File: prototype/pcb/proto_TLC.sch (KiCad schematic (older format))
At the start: 29 parts, among them Q1 RZM001P02, Q2 RZM001P02, Q3 RZM001P02, Q4 RZM001P02, U1 TLC5954

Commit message: Finished rectangular prototype board
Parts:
- renumbered C3 to C1, C1 to C2, C2 to C3, D4 to D10, D6 to D11, D8 to D12, D9 to D13, D11 to D14, D13 to D15, D15 to D16, D3 to D2, D5 to D3, D7 to D4, D10 to D5, D12 to D6, D14 to D7, D16 to D8, D2 to D9, R5 to R4, R4 to R5
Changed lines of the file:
@@
 $EndComp
 $Comp
-L APHB1608LVBDSEKJ3C D3
+L APHB1608LVBDSEKJ3C D2
 U 1 1 574E23F2
 P 6600 2850
-F 0 "D3" H 6400 3050 50  0000 L CNN
+F 0 "D2" H 6400 3050 50  0000 L CNN
 F 1 "APHB1608LVBDSEKJ3C" H 6550 2650 50  0000 C CNN
 F 2 "led:led_dual" H 6600 2800 60  0001 C CNN
@@
 $EndComp
 $Comp
-L APHB1608LVBDSEKJ3C D5
+L APHB1608LVBDSEKJ3C D3
 U 1 1 574E2426
 P 7200 2850
-F 0 "D5" H 7000 3050 50  0000 L CNN
+F 0 "D3" H 7000 3050 50  0000 L CNN
 F 1 "APHB1608LVBDSEKJ3C" H 7150 2650 50  0000 C CNN
 F 2 "led:led_dual" H 7200 2800 60  0001 C CNN
@@
 $EndComp
 $Comp
-L APHB1608LVBDSEKJ3C D7
+L APHB1608LVBDSEKJ3C D4
 U 1 1 574E245C
 P 7750 2850
-F 0 "D7" H 7550 3050 50  0000 L CNN
+F 0 "D4" H 7550 3050 50  0000 L CNN
 F 1 "APHB1608LVBDSEKJ3C" H 7700 2650 50  0000 C CNN
 F 2 "led:led_dual" H 7750 2800 60  0001 C CNN
@@
 $EndComp
 $Comp
-L APHB1608LVBDSEKJ3C D10
+L APHB1608LVBDSEKJ3C D5
 U 1 1 574E248E
 P 8350 2850
-F 0 "D10" H 8150 3050 50  0000 L CNN
+F 0 "D5" H 8150 3050 50  0000 L CNN
 F 1 "APHB1608LVBDSEKJ3C" H 8300 2650 50  0000 C CNN
 F 2 "led:led_dual" H 8350 2800 60  0001 C CNN
@@
 $EndComp
 $Comp
-L APHB1608LVBDSEKJ3C D12
+L APHB1608LVBDSEKJ3C D6
 U 1 1 574E24C0
 P 8900 2850
-F 0 "D12" H 8700 3050 50  0000 L CNN
+F 0 "D6" H 8700 3050 50  0000 L CNN
 F 1 "APHB1608LVBDSEKJ3C" H 8850 2650 50  0000 C CNN
 F 2 "led:led_dual" H 8900 2800 60  0001 C CNN
@@
 $EndComp
 $Comp
-L APHB1608LVBDSEKJ3C D14
+L APHB1608LVBDSEKJ3C D7
 U 1 1 574E38A4
 P 9500 2850
-F 0 "D14" H 9300 3050 50  0000 L CNN
+F 0 "D7" H 9300 3050 50  0000 L CNN
 F 1 "APHB1608LVBDSEKJ3C" H 9450 2650 50  0000 C CNN
 F 2 "led:led_dual" H 9500 2800 60  0001 C CNN
@@
 $EndComp
 $Comp
-L APHB1608LVBDSEKJ3C D16
+L APHB1608LVBDSEKJ3C D8
 U 1 1 574E38AA
 P 10050 2850
-F 0 "D16" H 9850 3050 50  0000 L CNN
+F 0 "D8" H 9850 3050 50  0000 L CNN
 F 1 "APHB1608LVBDSEKJ3C" H 10000 2650 50  0000 C CNN
 F 2 "led:led_dual" H 10050 2800 60  0001 C CNN
@@
 $EndComp
 $Comp
-L APHB1608LVBDSEKJ3C D2
+L APHB1608LVBDSEKJ3C D9
 U 1 1 574E38B0
 P 6050 4450
-F 0 "D2" H 5850 4650 50  0000 L CNN
+F 0 "D9" H 5850 4650 50  0000 L CNN
 F 1 "APHB1608LVBDSEKJ3C" H 6000 4250 50  0000 C CNN
 F 2 "led:led_dual" H 6050 4400 60  0001 C CNN
@@
 $EndComp
 $Comp
-L APHB1608LVBDSEKJ3C D4
+L APHB1608LVBDSEKJ3C D10
 U 1 1 574E38B6
 P 6600 4450
-F 0 "D4" H 6400 4650 50  0000 L CNN
+F 0 "D10" H 6400 4650 50  0000 L CNN
 F 1 "APHB1608LVBDSEKJ3C" H 6550 4250 50  0000 C CNN
 F 2 "led:led_dual" H 6600 4400 60  0001 C CNN
@@
 $EndComp
 $Comp
-L APHB1608LVBDSEKJ3C D6
+L APHB1608LVBDSEKJ3C D11
 U 1 1 574E38BC
 P 7200 4450
-F 0 "D6" H 7000 4650 50  0000 L CNN
+F 0 "D11" H 7000 4650 50  0000 L CNN
 F 1 "APHB1608LVBDSEKJ3C" H 7150 4250 50  0000 C CNN
 F 2 "led:led_dual" H 7200 4400 60  0001 C CNN
@@
 $EndComp
 $Comp
-L APHB1608LVBDSEKJ3C D8
+L APHB1608LVBDSEKJ3C D12
 U 1 1 574E38C2
 P 7750 4450
-F 0 "D8" H 7550 4650 50  0000 L CNN
+F 0 "D12" H 7550 4650 50  0000 L CNN
 F 1 "APHB1608LVBDSEKJ3C" H 7700 4250 50  0000 C CNN
 F 2 "led:led_dual" H 7750 4400 60  0001 C CNN
@@
 $EndComp
 $Comp
-L APHB1608LVBDSEKJ3C D9
+L APHB1608LVBDSEKJ3C D13
 U 1 1 574E41CA
 P 8300 4450
-F 0 "D9" H 8100 4650 50  0000 L CNN
+F 0 "D13" H 8100 4650 50  0000 L CNN
 F 1 "APHB1608LVBDSEKJ3C" H 8250 4250 50  0000 C CNN
 F 2 "led:led_dual" H 8300 4400 60  0001 C CNN
@@
 $EndComp
 $Comp
-L APHB1608LVBDSEKJ3C D11
+L APHB1608LVBDSEKJ3C D14
 U 1 1 574E41D0
 P 8850 4450
-F 0 "D11" H 8650 4650 50  0000 L CNN
+F 0 "D14" H 8650 4650 50  0000 L CNN
 F 1 "APHB1608LVBDSEKJ3C" H 8800 4250 50  0000 C CNN
 F 2 "led:led_dual" H 8850 4400 60  0001 C CNN
@@
 $EndComp
 $Comp
-L APHB1608LVBDSEKJ3C D13
+L APHB1608LVBDSEKJ3C D15
 U 1 1 574E41D6
 P 9450 4450
-F 0 "D13" H 9250 4650 50  0000 L CNN
+F 0 "D15" H 9250 4650 50  0000 L CNN
 F 1 "APHB1608LVBDSEKJ3C" H 9400 4250 50  0000 C CNN
 F 2 "led:led_dual" H 9450 4400 60  0001 C CNN
@@
 $EndComp
 $Comp
-L APHB1608LVBDSEKJ3C D15
+L APHB1608LVBDSEKJ3C D16
 U 1 1 574E41DC
 P 10000 4450
-F 0 "D15" H 9800 4650 50  0000 L CNN
+F 0 "D16" H 9800 4650 50  0000 L CNN
 F 1 "APHB1608LVBDSEKJ3C" H 9950 4250 50  0000 C CNN
 F 2 "led:led_dual" H 10000 4400 60  0001 C CNN
@@
 $EndComp
 $Comp
-L R R4
+L R R5
 U 1 1 574E48DB
 P 11800 2400
-F 0 "R4" V 11880 2400 50  0000 C CNN
+F 0 "R5" V 11880 2400 50  0000 C CNN
 F 1 "R" V 11800 2400 50  0000 C CNN
 F 2 "Resistors_SMD:R_0603" V 11730 2400 30  0001 C CNN
@@
 	2850 3500 2250 3500
 $Comp
-L R R5
+L R R4
 U 1 1 574EFA18
 P 2000 2300
-F 0 "R5" V 2080 2300 50  0000 C CNN
+F 0 "R4" V 2080 2300 50  0000 C CNN
 F 1 "R" V 2000 2300 50  0000 C CNN
 F 2 "Resistors_SMD:R_0603" V 1930 2300 30  0001 C CNN
@@
 LED_EN_3
 $Comp
-L C C1
+L C C2
 U 1 1 574F4CFC
 P 2550 2550
-F 0 "C1" H 2575 2650 50  0000 L CNN
+F 0 "C2" H 2575 2650 50  0000 L CNN
 F 1 "C" H 2575 2450 50  0000 L CNN
 F 2 "Capacitors_SMD:C_0603" H 2588 2400 30  0001 C CNN
@@
 	2550 2750 2550 2700
 $Comp
-L C C2
+L C C3
 U 1 1 574F5C22
 P 2800 2550
-F 0 "C2" H 2825 2650 50  0000 L CNN
+F 0 "C3" H 2825 2650 50  0000 L CNN
 F 1 "C" H 2825 2450 50  0000 L CNN
 F 2 "Capacitors_SMD:C_0603" H 2838 2400 30  0001 C CNN
@@
 Connection ~ 2550 2750
 $Comp
-L C C3
+L C C1
 U 1 1 574F60F7
 P 15200 2000
-F 0 "C3" H 15225 2100 50  0000 L CNN
+F 0 "C1" H 15225 2100 50  0000 L CNN
 F 1 "C" H 15225 1900 50  0000 L CNN
 F 2 "Capacitors_SMD:C_0603" H 15238 1850 30  0001 C CNN

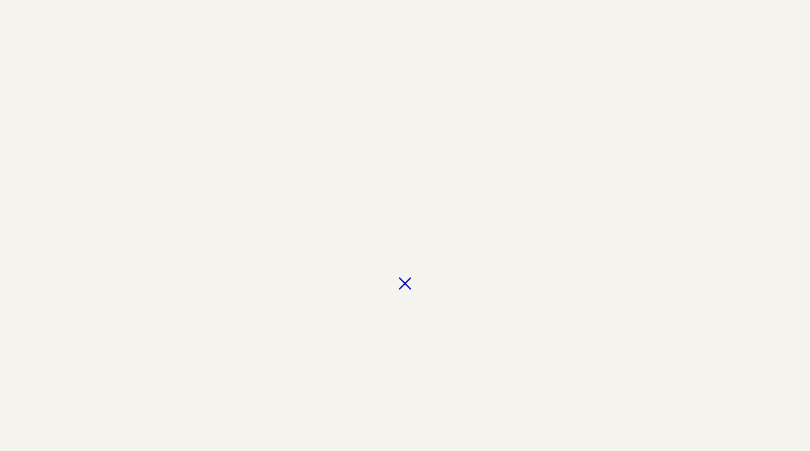
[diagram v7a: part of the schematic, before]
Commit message: Added concentric power traces
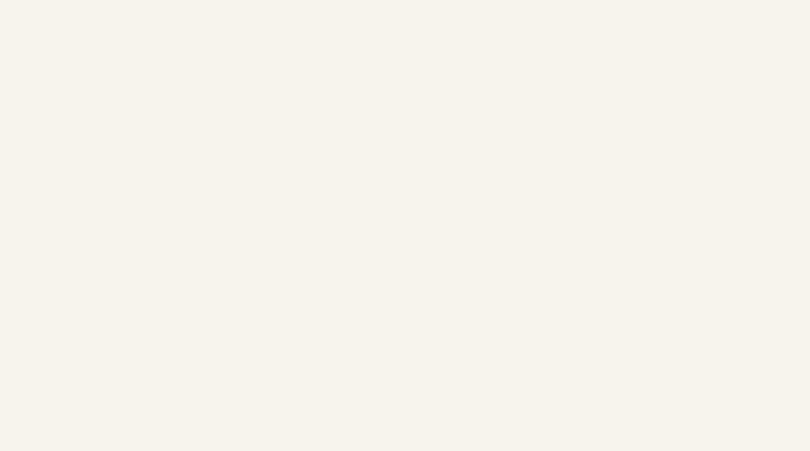
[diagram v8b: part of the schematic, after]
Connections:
- no-connect marks 42 -> 41
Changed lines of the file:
@@
 	6100 4900 6100 4650
-Wire Wire Line
-	5950 4650 5950 4900
 Wire Wire Line
 	6500 3050 6500 3300
@@
 Connection ~ 14600 1900
 NoConn ~ 4550 7300
-NoConn ~ 7700 8400
 Text HLabel 2250 3200 0    60   Input ~ 0
 SIN
@@
 Wire Wire Line
 	3650 8500 3650 8600
+Wire Wire Line
+	5950 4650 5950 4900
 $EndSCHEMATC
